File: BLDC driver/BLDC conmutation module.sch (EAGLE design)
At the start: 33 parts, among them Q1 INFINEON_IRFB3077PBFINFINEON_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, Q2 INFINEON_IRFB3077PBFINFINEON_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, Q3 INFINEON_IRFB3077PBFINFINEON_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, Q4 INFINEON_IRFB3077PBFINFINEON_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, Q5 INFINEON_IRFB3077PBFINFINEON_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, Q6 INFINEON_IRFB3077PBFINFINEON_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, U1 ESP32-DEVKIT-V1, U2 IR2183, U3 IR2183, U4 IR2183

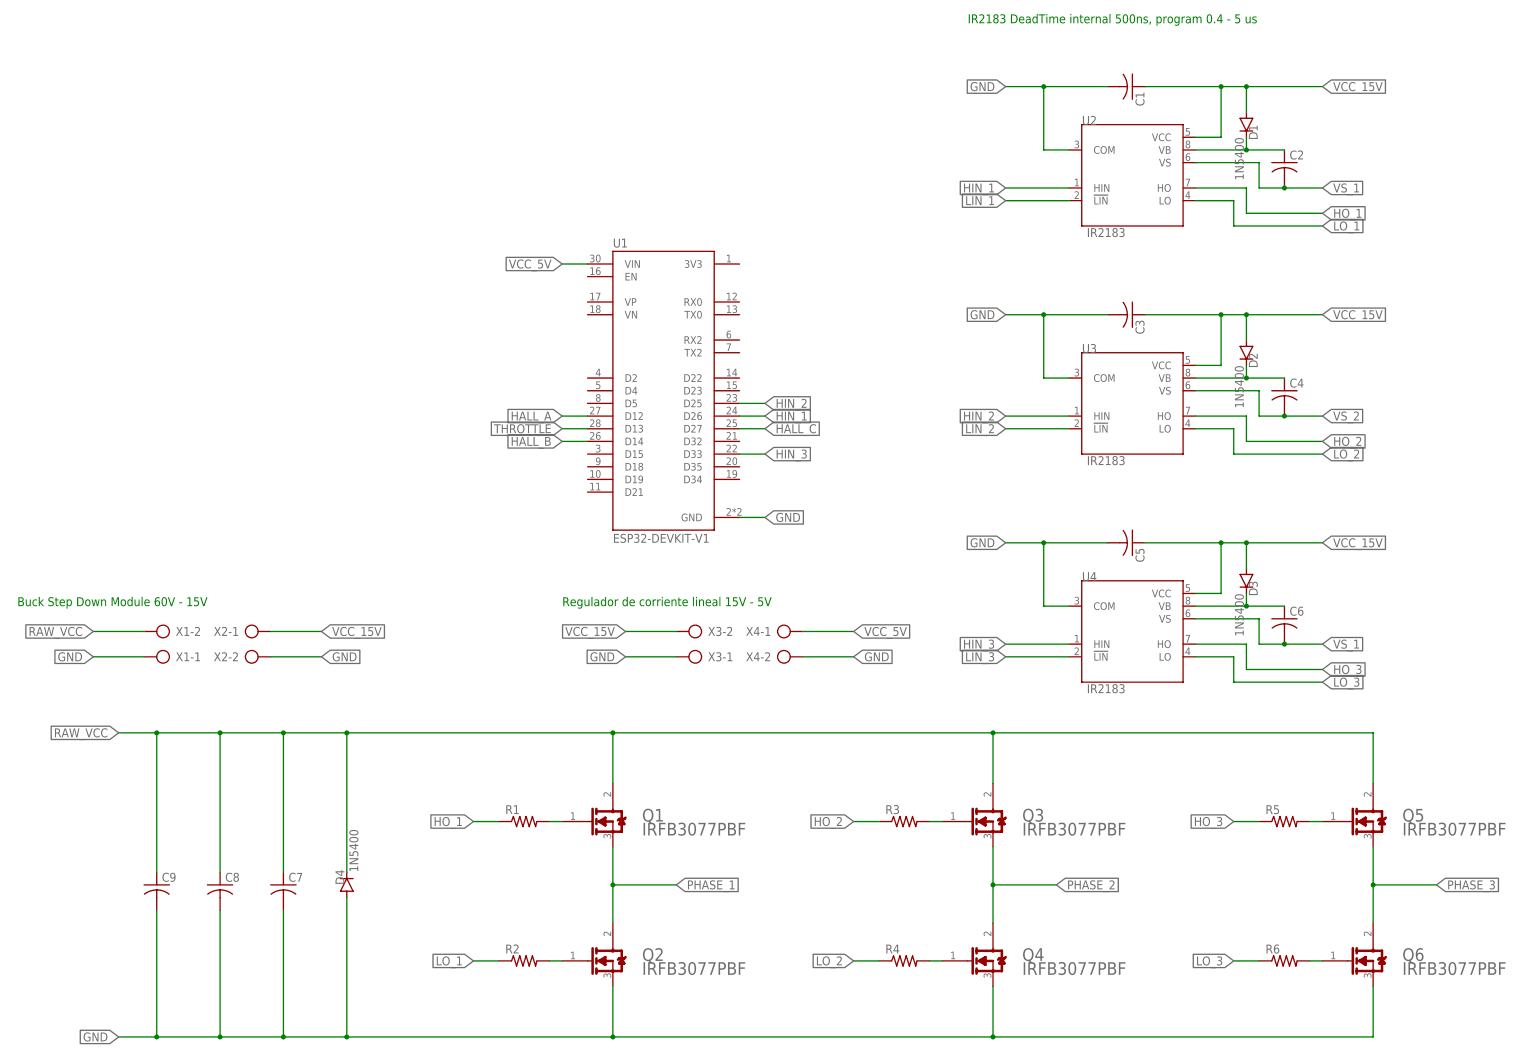
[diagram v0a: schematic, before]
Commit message: Actualizacion diseno controlador
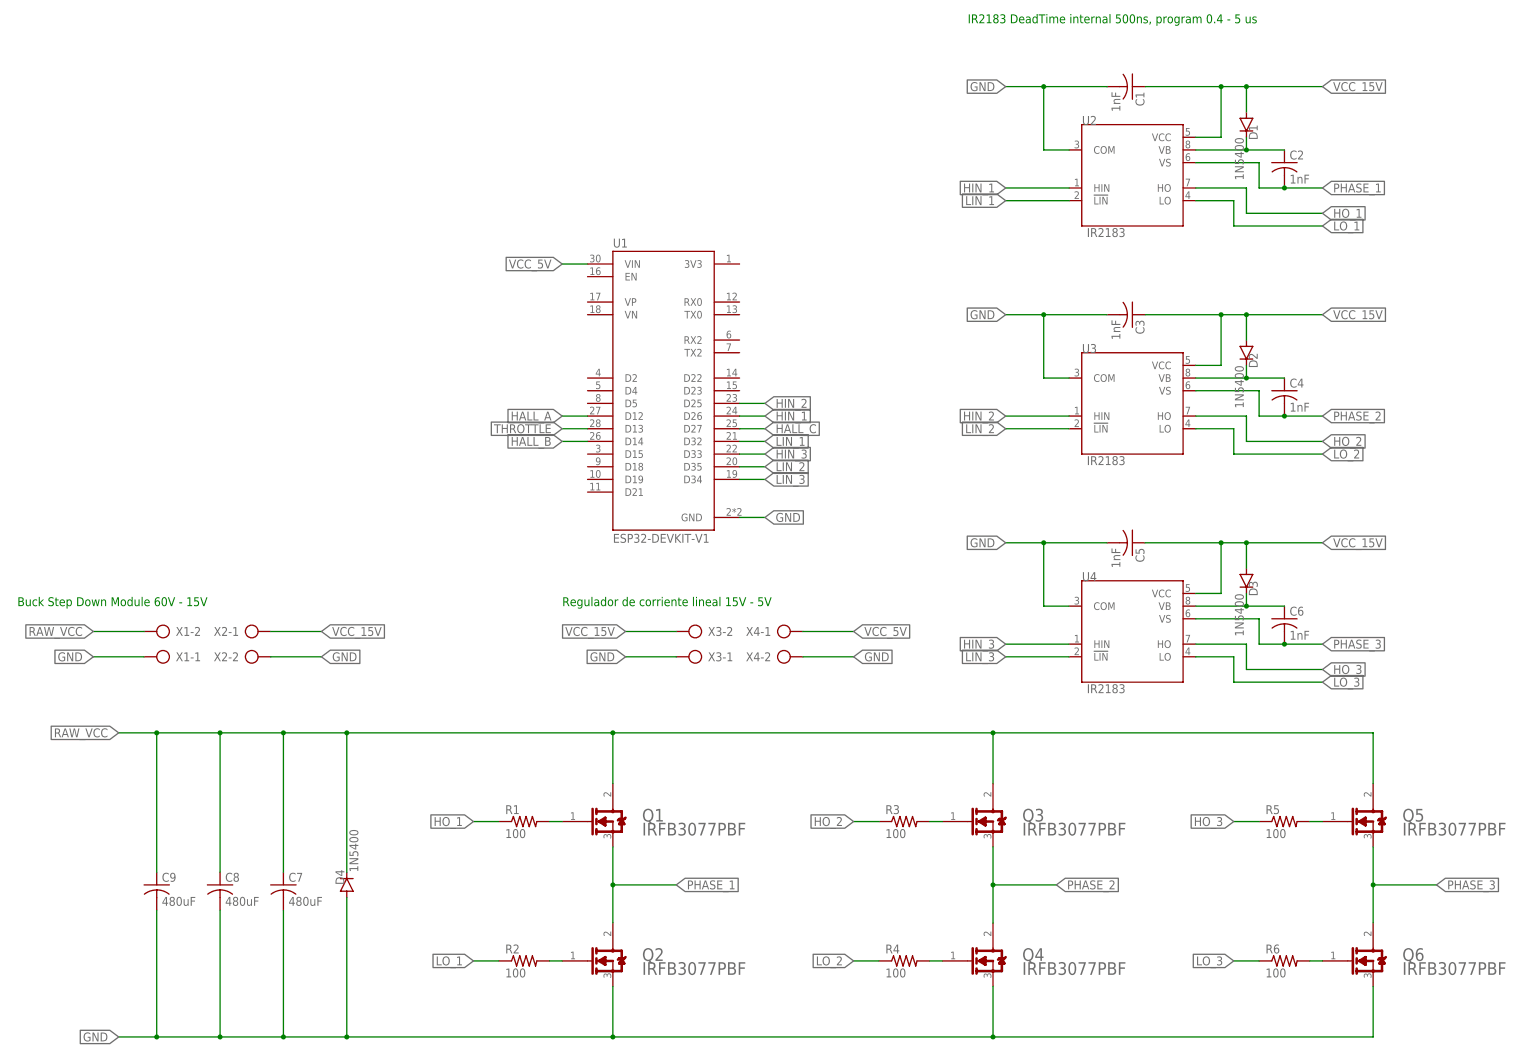
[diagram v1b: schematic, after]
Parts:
- C1, C2, C3, C4, C5, C6: value (none) -> 1nF
- C7, C8, C9: value (none) -> 480uF
- R1, R2, R3, R4, R5, R6: value (none) -> 100
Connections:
- removed net VS_1: C2.2, C6.2, U2.VS, U4.VS
- removed net VS_2: C4.2, U3.VS
- net LIN_1: now also U1.D32
- net LIN_2: now also U1.D35
- net LIN_3: now also U1.D34
- net PHASE_1: now also C2.2, U2.VS
- net PHASE_2: now also C4.2, U3.VS
- net PHASE_3: now also C6.2, U4.VS
